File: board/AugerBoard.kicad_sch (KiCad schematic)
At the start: 0 parts

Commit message: Edited names and locations for readability
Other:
- sheet Power ports: added SpareMotorLED; removed SpareLED
- sheet Teensy ports: added CacheSpareLED, SpareMotorLED; removed CacheSPareLED, SpareLED
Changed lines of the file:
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@@
+	(wire
+		(pts
+			(xy 161.29 99.06) (xy 166.37 99.06)
+		)
+		(stroke
+			(width 0)
+			(type default)
+		)
+	)
+	(wire
+		(pts
+			(xy 101.6 106.68) (xy 106.68 106.68)
+		)
+		(stroke
+			(width 0)
+			(type default)
+		)
+	)
+	(wire
+		(pts
+			(xy 161.29 93.98) (xy 166.37 93.98)
+		)
+		(stroke
+			(width 0)
+			(type default)
+		)
+	)
+	(wire
+		(pts
+			(xy 154.94 74.93) (xy 154.94 80.01)
+		)
+		(stroke
+			(width 0)
+			(type default)
+		)
+	)
+	(wire
+		(pts
+			(xy 101.6 101.6) (xy 106.68 101.6)
+		)
+		(stroke
+			(width 0)
+			(type default)
+		)
+	)
+	(wire
+		(pts
+			(xy 101.6 119.38) (xy 106.68 119.38)
+		)
+		(stroke
+			(width 0)
+			(type default)
+		)
+	)
+	(wire
+		(pts
+			(xy 149.86 74.93) (xy 149.86 80.01)
+		)
+		(stroke
+			(width 0)
+			(type default)
+		)
+	)
+	(wire
+		(pts
+			(xy 124.46 125.73) (xy 124.46 130.81)
+		)
+		(stroke
+			(width 0)
+			(type default)
+		)
+	)
+	(wire
+		(pts
+			(xy 101.6 81.28) (xy 106.68 81.28)
+		)
+		(stroke
+			(width 0)
+			(type default)
+		)
+	)
+	(wire
+		(pts
+			(xy 157.48 74.93) (xy 157.48 80.01)
+		)
+		(stroke
+			(width 0)
+			(type default)
+		)
+	)
+	(wire
+		(pts
+			(xy 129.54 125.73) (xy 129.54 130.81)
+		)
+		(stroke
+			(width 0)
+			(type default)
+		)
+	)
+	(wire
+		(pts
+			(xy 101.6 121.92) (xy 106.68 121.92)
+		)
+		(stroke
+			(width 0)
+			(type default)
+		)
+	)
+	(wire
+		(pts
+			(xy 160.02 125.73) (xy 160.02 130.81)
+		)
+		(stroke
+			(width 0)
+			(type default)
+		)
+	)
+	(wire
+		(pts
+			(xy 161.29 91.44) (xy 166.37 91.44)
+		)
+		(stroke
+			(width 0)
+			(type default)
+		)
+	)
+	(wire
+		(pts
+			(xy 101.6 91.44) (xy 106.68 91.44)
+		)
+		(stroke
+			(width 0)
+			(type default)
+		)
+	)
+	(wire
+		(pts
+			(xy 152.4 125.73) (xy 152.4 130.81)
+		)
+		(stroke
+			(width 0)
+			(type default)
+		)
+	)
+	(wire
+		(pts
+			(xy 101.6 86.36) (xy 106.68 86.36)
+		)
+		(stroke
+			(width 0)
+			(type default)
+		)
+	)
+	(wire
+		(pts
+			(xy 101.6 93.98) (xy 106.68 93.98)
+		)
+		(stroke
+			(width 0)
+			(type default)
+		)
+	)
+	(wire
+		(pts
+			(xy 101.6 104.14) (xy 106.68 104.14)
+		)
+		(stroke
+			(width 0)
+			(type default)
+		)
+	)
+	(wire
+		(pts
+			(xy 144.78 74.93) (xy 144.78 80.01)
+		)
+		(stroke
+			(width 0)
+			(type default)
+		)
+	)
+	(wire
+		(pts
+			(xy 139.7 125.73) (xy 139.7 130.81)
+		)
+		(stroke
+			(width 0)
+			(type default)
+		)
+	)
 	(wire
 		(pts
@@
 	(wire
 		(pts
-			(xy 161.29 99.06) (xy 166.37 99.06)
-		)
-		(stroke
-			(width 0)
-			(type default)
-		)
-	)
-	(wire
-		(pts
-			(xy 101.6 106.68) (xy 106.68 106.68)
-		)
-		(stroke
-			(width 0)
-			(type default)
-		)
-	)
-	(wire
-		(pts
-			(xy 161.29 93.98) (xy 166.37 93.98)
-		)
-		(stroke
-			(width 0)
-			(type default)
-		)
-	)
-	(wire
-		(pts
-			(xy 154.94 74.93) (xy 154.94 80.01)
+			(xy 101.6 114.3) (xy 106.68 114.3)
 		)
 		(stroke
@@
 		(pts
 			(xy 142.24 125.73) (xy 142.24 130.81)
-		)
-		(stroke
-			(width 0)
-			(type default)
-		)
-	)
-	(wire
-		(pts
-			(xy 101.6 101.6) (xy 106.68 101.6)
-		)
-		(stroke
-			(width 0)
-			(type default)
-		)
-	)
-	(wire
-		(pts
-			(xy 101.6 119.38) (xy 106.68 119.38)
-		)
-		(stroke
-			(width 0)
-			(type default)
-		)
-	)
-	(wire
-		(pts
-			(xy 149.86 74.93) (xy 149.86 80.01)
-		)
-		(stroke
-			(width 0)
-			(type default)
-		)
-	)
-	(wire
-		(pts
-			(xy 124.46 125.73) (xy 124.46 130.81)
-		)
-		(stroke
-			(width 0)
-			(type default)
-		)
-	)
-	(wire
-		(pts
-			(xy 139.7 125.73) (xy 139.7 130.81)
-		)
-		(stroke
-			(width 0)
-			(type default)
-		)
-	)
-	(wire
-		(pts
-			(xy 101.6 81.28) (xy 106.68 81.28)
-		)
-		(stroke
-			(width 0)
-			(type default)
-		)
-	)
-	(wire
-		(pts
-			(xy 157.48 74.93) (xy 157.48 80.01)
-		)
-		(stroke
-			(width 0)
-			(type default)
-		)
-	)
-	(wire
-		(pts
-			(xy 129.54 125.73) (xy 129.54 130.81)
-		)
-		(stroke
-			(width 0)
-			(type default)
-		)
-	)
-	(wire
-		(pts
-			(xy 101.6 121.92) (xy 106.68 121.92)
-		)
-		(stroke
-			(width 0)
-			(type default)
-		)
-	)
-	(wire
-		(pts
-			(xy 160.02 125.73) (xy 160.02 130.81)
-		)
-		(stroke
-			(width 0)
-			(type default)
-		)
-	)
-	(wire
-		(pts
-			(xy 161.29 91.44) (xy 166.37 91.44)
-		)
-		(stroke
-			(width 0)
-			(type default)
-		)
-	)
-	(wire
-		(pts
-			(xy 101.6 91.44) (xy 106.68 91.44)
-		)
-		(stroke
-			(width 0)
-			(type default)
-		)
-	)
-	(wire
-		(pts
-			(xy 152.4 125.73) (xy 152.4 130.81)
-		)
-		(stroke
-			(width 0)
-			(type default)
-		)
-	)
-	(wire
-		(pts
-			(xy 101.6 86.36) (xy 106.68 86.36)
-		)
-		(stroke
-			(width 0)
-			(type default)
-		)
-	)
-	(wire
-		(pts
-			(xy 101.6 93.98) (xy 106.68 93.98)
-		)
-		(stroke
-			(width 0)
-			(type default)
-		)
-	)
-	(wire
-		(pts
-			(xy 101.6 104.14) (xy 106.68 104.14)
-		)
-		(stroke
-			(width 0)
-			(type default)
-		)
-	)
-	(wire
-		(pts
-			(xy 144.78 74.93) (xy 144.78 80.01)
-		)
-		(stroke
-			(width 0)
-			(type default)
-		)
-	)
-	(wire
-		(pts
-			(xy 101.6 114.3) (xy 106.68 114.3)
 		)
 		(stroke
@@
 			)
 		)
-		(pin "SpareLED" output
+		(pin "SpareMotorLED" output
 			(at 157.48 125.73 270)
 			(effects
@@
 			)
 		)
-		(pin "CacheSPareLED" output
+		(pin "CacheSpareLED" output
 			(at 147.32 125.73 270)
 			(effects
@@
 	)
 	(sheet
-		(at 140.97 59.69)
-		(size 20.32 15.24)
+		(at 106.68 59.69)
+		(size 54.61 15.24)
 		(exclude_from_sim no)
 		(in_bom yes)
@@
 		)
 		(property "Sheetname" "Communications"
-			(at 140.2584 74.93 90)
+			(at 105.9684 74.93 90)
 			(effects
 				(font
@@
 			)
 		)
-		(pin "SpareLED" input
+		(pin "SpareMotorLED" input
 			(at 157.48 130.81 90)
 			(effects
@@
 		)
 		(pin "SoilTDLED" input
+			(at 139.7 130.81 90)
+			(effects
+				(font
+					(size 1.27 1.27)
+				)
+				(justify right)
+			)
+		)
+		(pin "SpareServoLED1" input
 			(at 144.78 130.81 90)
 			(effects
@@
 			)
 		)
-		(pin "SpareServoLED1" input
+		(pin "SpareServoLED2" input
 			(at 142.24 130.81 90)
 			(effects
 				(font
-					(size 1.27 1.27)
-				)
-				(justify right)
-			)
-		)
-		(pin "SpareServoLED2" input
-			(at 139.7 130.81 90)
-			(effects
-				(font

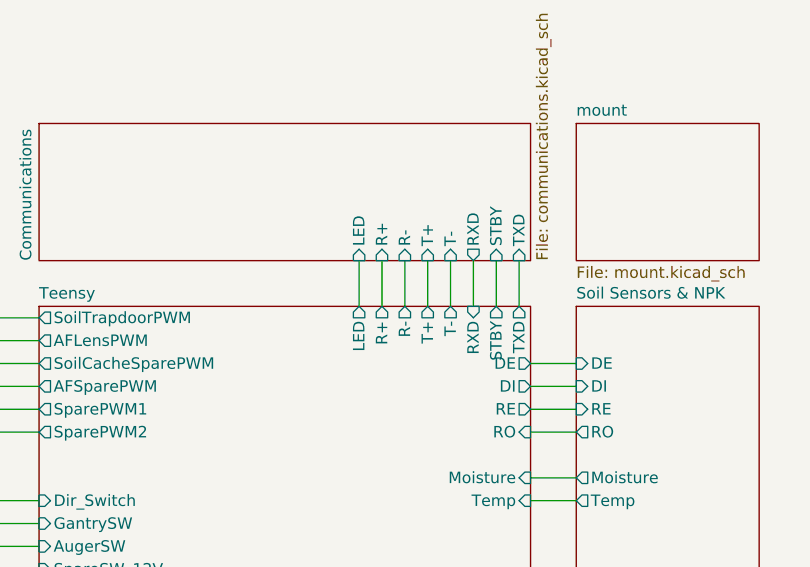
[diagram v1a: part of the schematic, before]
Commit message: Added second CAN tranceiver and a switch
also imported a new symbol for both the switch symbol and its footprint
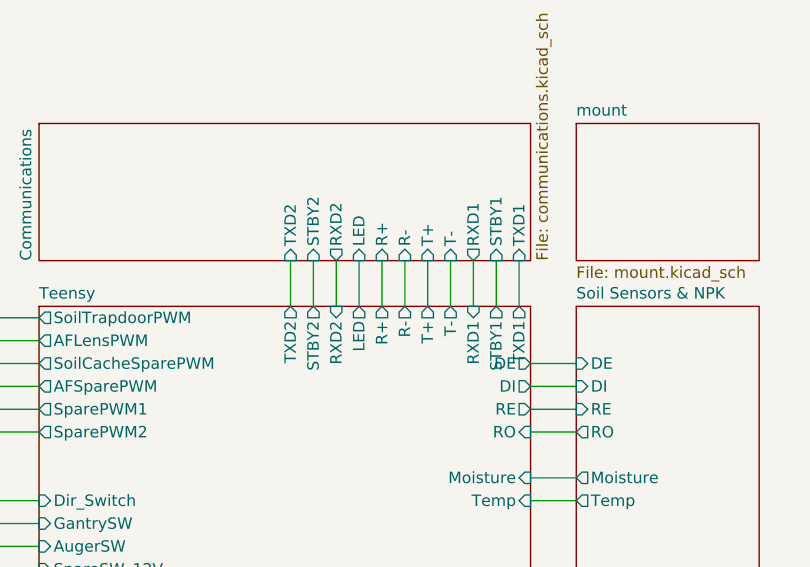
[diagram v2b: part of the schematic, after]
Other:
- sheet Communications ports: added RXD1, RXD2, STBY1, STBY2, TXD1, TXD2; removed RXD, STBY, TXD
- sheet Teensy ports: added RXD1, RXD2, STBY1, STBY2, TXD1, TXD2; removed RXD, STBY, TXD
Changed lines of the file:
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@@
+	(wire
+		(pts
+			(xy 134.62 74.93) (xy 134.62 80.01)
+		)
+		(stroke
+			(width 0)
+			(type default)
+		)
+	)
 	(wire
 		(pts
@@
 	(wire
 		(pts
+			(xy 137.16 74.93) (xy 137.16 80.01)
+		)
+		(stroke
+			(width 0)
+			(type default)
+		)
+	)
+	(wire
+		(pts
 			(xy 152.4 125.73) (xy 152.4 130.81)
 		)
@@
 		(pts
 			(xy 142.24 125.73) (xy 142.24 130.81)
+		)
+		(stroke
+			(width 0)
+			(type default)
+		)
+	)
+	(wire
+		(pts
+			(xy 139.7 74.93) (xy 139.7 80.01)
 		)
 		(stroke
@@
 			)
 		)
-		(pin "RXD" input
+		(pin "RXD1" input
 			(at 154.94 80.01 90)
 			(effects
@@
 			)
 		)
-		(pin "STBY" output
+		(pin "STBY1" output
 			(at 157.48 80.01 90)
 			(effects
@@
 			)
 		)
-		(pin "TXD" output
+		(pin "TXD1" output
 			(at 160.02 80.01 90)
 			(effects
@@
 				)
 				(justify left)
+			)
+		)
+		(pin "RXD2" input
+			(at 139.7 80.01 90)
+			(effects
+				(font
+					(size 1.27 1.27)
+				)
+				(justify right)
+			)
+		)
+		(pin "STBY2" output
+			(at 137.16 80.01 90)
+			(effects
+				(font
+					(size 1.27 1.27)
+				)
+				(justify right)
+			)
+		)
+		(pin "TXD2" output
+			(at 134.62 80.01 90)
+			(effects
+				(font
+					(size 1.27 1.27)
+				)
+				(justify right)
 			)
 		)
@@
 			)
 		)
-		(pin "RXD" output
+		(pin "RXD1" output
 			(at 154.94 74.93 270)
 			(effects
@@
 			)
 		)
-		(pin "STBY" input
+		(pin "STBY1" input
 			(at 157.48 74.93 270)
 			(effects
@@
 			)
 		)
-		(pin "TXD" input
+		(pin "TXD1" input
 			(at 160.02 74.93 270)
+			(effects
+				(font
+					(size 1.27 1.27)
+				)
+				(justify left)
+			)
+		)
+		(pin "RXD2" output
+			(at 139.7 74.93 270)
+			(effects
+				(font
+					(size 1.27 1.27)
+				)
+				(justify left)
+			)
+		)
+		(pin "STBY2" input
+			(at 137.16 74.93 270)
+			(effects
+				(font
+					(size 1.27 1.27)
+				)
+				(justify left)
+			)
+		)
+		(pin "TXD2" input
+			(at 134.62 74.93 270)
 			(effects
 				(font
@@
 	)
 	(embedded_fonts no)
+	(embedded_files
+		(file
+			(name "SOIC8_4P9X3P9MC_MCH.kicad_mod")
+			(type other)
+			(data |KLUv/WBEF9UXAHbZUCAQlR5qERaago/66eHUDmaTBIqQsbasZPr4FCIiAEKA4koARwBHAIhqXvYi
+				SAjQNQZv6CnEA/T8IryZ3AEBCvTeRet4/jbO7z1mcqpOOSeV1L2v0/k/k8NEYWEpLDKHRckc1XIL
+				ikYE+va63Nnfx00BM0rX+j2N1mX25NT06T/q9OTb+7jJ9dae435yj2g2XSQeqO012rfxPC5dOhwM
+				DgYI9Ne8z8999h36belwG0d73hs7o5o8CAFWlDeT0aKqpTJKz+ytA01OQWhnpJv39rrWZhlvPfl7
+				3SarmHUrZuO8l7yiVfnFJhZpBUuGAsMAMZAE0PNrzwUf/D0b/KEoG4AAdbHLVsu6oqRQo/Hit8YO
+				fem8lJV3a59942iHE/qGO9ZVpW8dp0ot42lrdemVcNqbSUrt3Co7V/VaNVKvV2L3RnkDgM2ogRoh
+				EpGClCSFwjIGUE4gIze1OWIwJIaiEKwAQhCGgCFgIgEhRNCEEyIgSEAI3A6SqpGNmn+nliT5bHv0
+				oWM7Ec0/NuHDDEEYsE0JLaqBZXBgKoFhhk+MCg6h5y6zKh6E5gxQ18irSHqRmlhavhtph3OR/m6K
+				YnX+HudchUFvnGs1WuaLz5tcE6R+NwmeLIlV4nAfEmXF6Q/Q8V2BD+NGa1y9gELEXwvr5pda+eWY
+				6BSk//ZFSP6J4UrnWB3rBCgC/9s4ehmx9pkDyWFDirwBRpGdIH/aBk+iR17EMikN7qcSQKT2PW+A
+				lQazKVbvRickKlBaxewrkeELBC2OHQYpS0T0s09WfcHIR79y7WKEzL9WLTfdz6jtKdizU1tasfY/
+				M2tDVzEPXsXjDvhdn76eBBDwgr/b2J8qMrBAWhwbsWCrdXwdvuDu2seysadGEBb3l5p+XCPyRx25
+				AIjoam7UmVOzfbcBXcCrFrnBcTFYaGCuN/kMzA6YGaT++CXJLIit6ztmQ7xR0y+IhqIsovDo0iT6
+				gAhgnGD6BjjSs4CtjzpknOzZKbbyH2Sl3zV1lbVXAQ==|
+			)
+			(checksum "A817AA0AA84CA29AFBD6893BF1836AEB")
+		)
+	)
 )

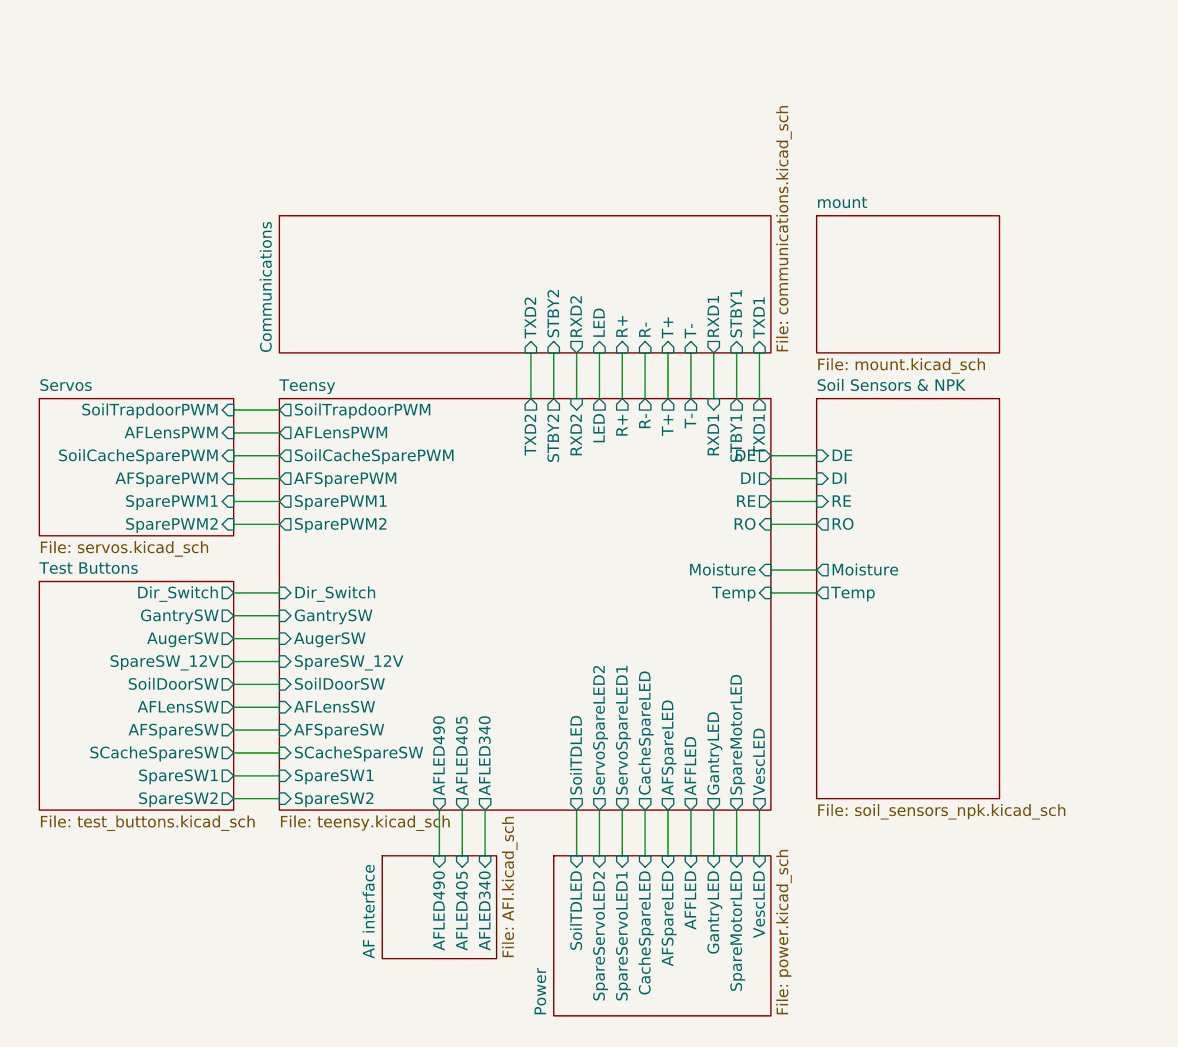
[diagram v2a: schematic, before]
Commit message: added pin for AF, added gimbal names, refined look
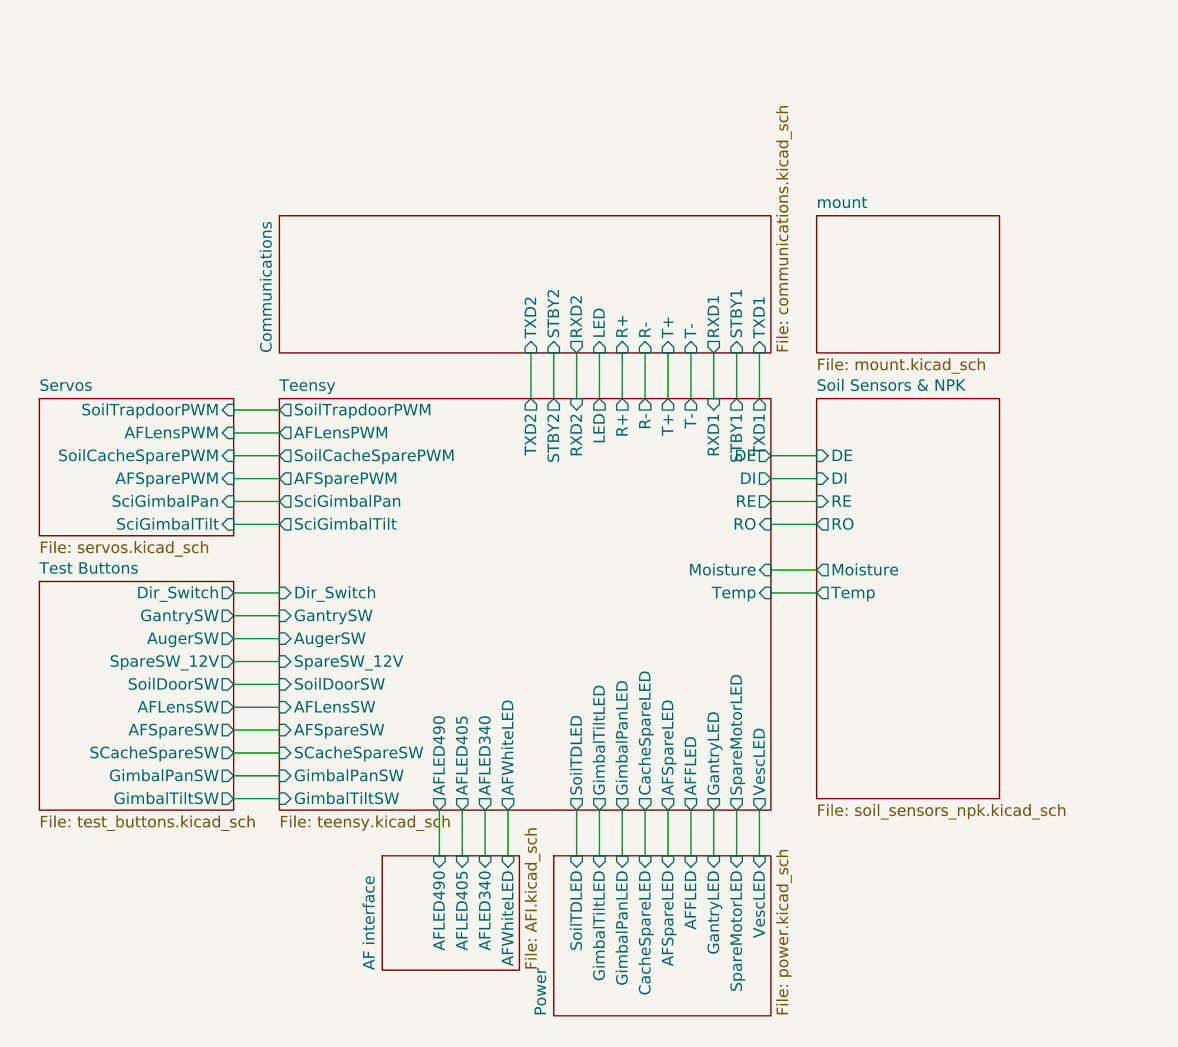
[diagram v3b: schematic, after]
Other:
- sheet AF interface ports: added AFWhiteLED; removed none
- sheet Power ports: added GimbalPanLED, GimbalTiltLED; removed SpareServoLED1, SpareServoLED2
- sheet Servos ports: added SciGimbalPan, SciGimbalTilt; removed SparePWM1, SparePWM2
- sheet Teensy ports: added AFWhiteLED, GimbalPanLED, GimbalPanSW, GimbalTiltLED, GimbalTiltSW, SciGimbalPan, SciGimbalTilt; removed ServoSpareLED1, ServoSpareLED2, SparePWM1, SparePWM2, SpareSW1, SpareSW2
- sheet Test Buttons ports: added GimbalPanSW, GimbalTiltSW; removed SpareSW1, SpareSW2
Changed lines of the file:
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@@
+	(wire
+		(pts
+			(xy 132.08 125.73) (xy 132.08 130.81)
+		)
+		(stroke
+			(width 0)
+			(type default)
+		)
+	)
 	(wire
 		(pts
@@
 			)
 		)
-		(pin "SparePWM1" output
+		(pin "SciGimbalPan" output
 			(at 106.68 91.44 180)
 			(effects
@@
 			)
 		)
-		(pin "SparePWM2" output
+		(pin "SciGimbalTilt" output
 			(at 106.68 93.98 180)
 			(effects
@@
 			)
 		)
-		(pin "SpareSW1" input
+		(pin "GimbalPanSW" input
 			(at 106.68 121.92 180)
 			(effects
@@
 			)
 		)
-		(pin "SpareSW2" input
+		(pin "GimbalTiltSW" input
 			(at 106.68 124.46 180)
 			(effects
@@
 			)
 		)
-		(pin "ServoSpareLED1" output
+		(pin "GimbalPanLED" output
 			(at 144.78 125.73 270)
 			(effects
@@
 			)
 		)
-		(pin "ServoSpareLED2" output
+		(pin "GimbalTiltLED" output
 			(at 142.24 125.73 270)
 			(effects
@@
 				)
 				(justify right)
+			)
+		)
+		(pin "AFWhiteLED" output
+			(at 132.08 125.73 270)
+			(effects
+				(font
+					(size 1.27 1.27)
+				)
+				(justify left)
 			)
 		)
@@
 			)
 		)
-		(pin "SpareServoLED1" input
+		(pin "GimbalPanLED" input
 			(at 144.78 130.81 90)
 			(effects
@@
 			)
 		)
-		(pin "SpareServoLED2" input
+		(pin "GimbalTiltLED" input
 			(at 142.24 130.81 90)
 			(effects
@@
 			)
 		)
-		(pin "SparePWM1" input
+		(pin "SciGimbalPan" input
 			(at 101.6 91.44 0)
 			(effects
@@
 			)
 		)
-		(pin "SparePWM2" input
+		(pin "SciGimbalTilt" input
 			(at 101.6 93.98 0)
 			(effects
@@
 			)
 		)
-		(pin "SpareSW1" output
+		(pin "GimbalPanSW" output
 			(at 101.6 121.92 0)
 			(effects
@@
 			)
 		)
-		(pin "SpareSW2" output
+		(pin "GimbalTiltSW" output
 			(at 101.6 124.46 0)
 			(effects
@@
 	(sheet
 		(at 118.11 130.81)
-		(size 12.7 11.43)
+		(size 15.24 12.7)
 		(exclude_from_sim no)
 		(in_bom yes)
@@
 		)
 		(property "Sheetname" "AF interface"
-			(at 117.3984 142.24 90)
+			(at 117.3984 143.51 90)
 			(effects
 				(font
@@
 		)
 		(property "Sheetfile" "AFI.kicad_sch"
-			(at 131.3946 142.24 90)
+			(at 133.9346 143.51 90)
 			(effects
 				(font
@@
 			(effects
 				(font
+					(size 1.27 1.27)
+				)
+				(justify right)
+			)
+		)
+		(pin "AFWhiteLED" input
+			(at 132.08 130.81 90)
+			(effects
+				(font

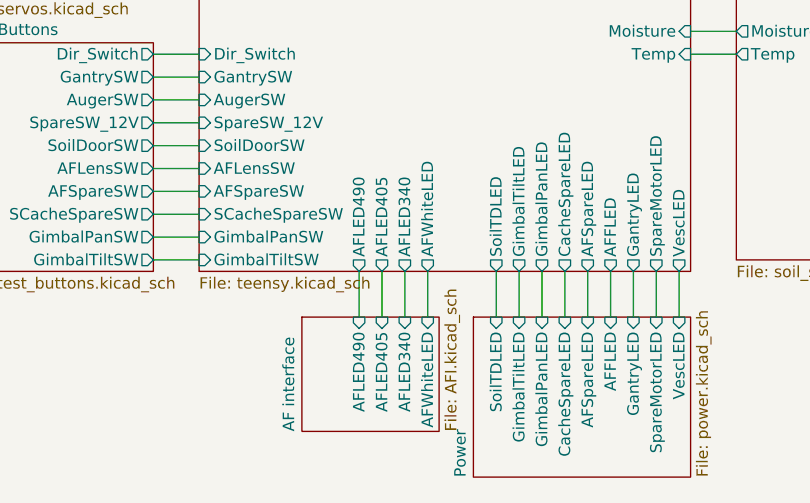
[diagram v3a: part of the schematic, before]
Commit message: Caught mislabeled pinout for AF after the recent pin change
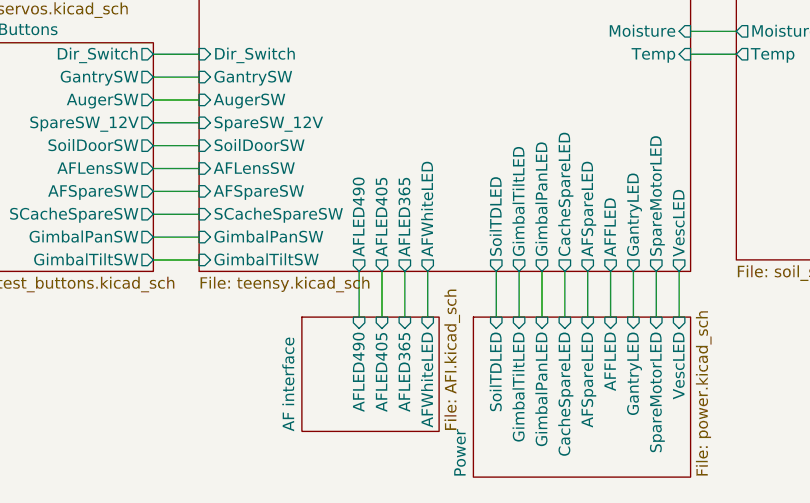
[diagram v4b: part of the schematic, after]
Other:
- sheet AF interface ports: added AFLED365; removed AFLED340
- sheet Teensy ports: added AFLED365; removed AFLED340
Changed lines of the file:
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@@
 			)
 		)
-		(pin "AFLED340" output
+		(pin "AFLED365" output
 			(at 129.54 125.73 270)
 			(effects
@@
 			)
 		)
-		(pin "AFLED340" input
+		(pin "AFLED365" input
 			(at 129.54 130.81 90)
 			(effects
